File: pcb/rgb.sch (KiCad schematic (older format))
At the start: 14 parts, among them J1 Conn_02x08_Odd_Even, J2 Conn_01x06, J3 Conn_01x02, U1 ESP-WROOM-32, U2 LM317EMP, U3 RASPI_SD

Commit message: Minimum example to show 1 (sub)frame for debugging
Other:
- note added: "First prototype has B0 here"
- note added: "First prototype has D here"
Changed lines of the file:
@@
 	1    0    0    -1
 $EndComp
+Text Notes 7800 2600 0    60   ~ 0
+First prototype has D here
+Text Notes 6550 4200 3    60   ~ 0
+First prototype has B0 here
 $EndSCHEMATC

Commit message: SD card is online and integrated into webserver
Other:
- note added: "First prototype CS"
- note added: "REV1 CS"
- note added: "REV1 MISO"
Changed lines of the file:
@@
 U 1 1 5A206FDA
 P 5200 3200
-F 0 "R4" V 5100 3000 50  0000 C CNN
-F 1 "10k" V 5084 3200 50  0000 C CNN
+F 0 "R4" V 5300 3050 50  0000 C CNN
+F 1 "10k" V 5300 3250 50  0000 C CNN
 F 2 "Resistors_SMD:R_0805" V 5130 3200 50  0001 C CNN
 F 3 "" H 5200 3200 50  0001 C CNN
@@
 Text Notes 6550 4200 3    60   ~ 0
 First prototype has B0 here
+Text Notes 4550 3100 0    60   ~ 0
+First prototype CS
+Text Notes 5400 3700 0    60   ~ 0
+REV1 CS
+Text Notes 5300 3800 0    60   ~ 0
+REV1 MISO
 $EndSCHEMATC

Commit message: PCB REV1
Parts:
- removed J2: Conn_01x06, myStuff:myPogoPads, symbol rgb-rescue:Conn_01x06-RESCUE-rgb
- added C5: 1u, Capacitors_SMD:C_0805, symbol Device:C
- added J2: Conn_01x02, Pin_Headers:Pin_Header_Angled_1x02_Pitch2.54mm, symbol rgb-rescue:Conn_01x02-RESCUE-rgb
- added P1: TTL_232R_3V3, Pin_Headers:Pin_Header_Angled_1x06_Pitch2.54mm, symbol myStuff:TTL_232R_3V3
- added R6: 10k, Resistors_SMD:R_0805, symbol Device:R
- added U4, U5: TACTILE, myStuff:EVQQ2, symbol myStuff:TACTILE
- C4: renamed from C?; symbol device:C -> Device:C
- R2, R3: renamed from R?; footprint (none) -> Resistors_SMD:R_0805; symbol device:R -> Device:R
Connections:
- wire segments 91 -> 133
- no-connect marks 14 -> 13
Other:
- note added: "Flash"
- note added: "Photo\nresistor"
- note added: "Reset"
- note removed: "5 V"
- note removed: "First prototype CS"
- note removed: "First prototype has B0 here"
- note removed: "First prototype has D here"
- note removed: "GND"
- note removed: "REV1 CS"
- note removed: "REV1 MISO"
- note removed: "RXD"
- note removed: "Rst"
- note removed: "TXD"

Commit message: final pcb with second sd card slot and kicad 5
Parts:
- added U6: MicroSD_SPI_CD, newStuff:GCT-MEM2055-00-190-01-A, symbol microsd_spi_cd:MicroSD_SPI_CD
- C1, C2, C3: symbol rgb-rescue:C-RESCUE-rgb -> Device:C
- J1: symbol rgb-rescue:Conn_02x08_Odd_Even-RESCUE-rgb -> Connector_Generic:Conn_02x08_Odd_Even
- J2, J3: symbol rgb-rescue:Conn_01x02-RESCUE-rgb -> Connector_Generic:Conn_01x02
- R1, R4: symbol rgb-rescue:R-RESCUE-rgb -> Device:R
- U1: symbol rgb-rescue:ESP-WROOM-32-RESCUE-rgb -> myStuff:ESP-WROOM-32
- U2: symbol rgb-rescue:LM317EMP-RESCUE-rgb -> myStuff:LM317EMP
- U3: symbol rgb-rescue:RASPI_SD-RESCUE-rgb -> myStuff:RASPI_SD
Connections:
- wire segments 133 -> 139
- no-connect marks 13 -> 14
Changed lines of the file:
@@
 $EndDescr
 $Comp
-L rgb-rescue:+3V3-RESCUE-rgb #PWR01
+L power:+3.3V #PWR01
 U 1 1 5A1F09A4
 P 5400 2450
@@
 $EndComp
 $Comp
-L rgb-rescue:C-RESCUE-rgb C1
+L Device:C C1
 U 1 1 5A1F09A5
 P 5600 2500
@@
 $EndComp
 $Comp
-L rgb-rescue:GND-RESCUE-rgb #PWR02
+L power:GND #PWR02
 U 1 1 5A1F09A6
 P 5800 2500
@@
 $EndComp
 $Comp
-L rgb-rescue:GND-RESCUE-rgb #PWR03
+L power:GND #PWR03
 U 1 1 5A1F09A7
 P 7850 2450
@@
 $EndComp
 $Comp
-L rgb-rescue:ESP-WROOM-32-RESCUE-rgb U1
+L myStuff:ESP-WROOM-32 U1
 U 1 1 5A1F09A8
 P 6750 3150
@@
 $EndComp
 $Comp
-L rgb-rescue:R-RESCUE-rgb R1
+L Device:R R1
 U 1 1 5A1F09AB
 P 5200 2500
@@
 rstBtn
 $Comp
-L rgb-rescue:GND-RESCUE-rgb #PWR04
+L power:GND #PWR04
 U 1 1 5A1F09AC
 P 6400 4200
@@
 $EndComp
 $Comp
-L rgb-rescue:GND-RESCUE-rgb #PWR05
+L power:GND #PWR05
 U 1 1 5A1F09AD
 P 9400 3150
@@
 progFlag
 $Comp
-L rgb-rescue:LM317EMP-RESCUE-rgb U2
+L myStuff:LM317EMP U2
 U 1 1 5A1F2D82
 P 3100 6450
@@
 $EndComp
 $Comp
-L rgb-rescue:+3V3-RESCUE-rgb #PWR06
+L power:+3.3V #PWR06
 U 1 1 5A1F32B5
 P 4500 6350
@@
 $EndComp
 $Comp
-L rgb-rescue:GND-RESCUE-rgb #PWR07
+L power:GND #PWR07
 U 1 1 5A1F370A
 P 3950 7200
@@
 $EndComp
 $Comp
-L rgb-rescue:GND-RESCUE-rgb #PWR08
+L power:GND #PWR08
 U 1 1 5A1F3E37
 P 2550 7200
@@
 $EndComp
 $Comp
-L rgb-rescue:Conn_01x02-RESCUE-rgb J3
+L Connector_Generic:Conn_01x02 J3
 U 1 1 5A1F3E67
 P 1950 6750
@@
 $EndComp
 $Comp
-L rgb-rescue:GND-RESCUE-rgb #PWR09
+L power:GND #PWR09
 U 1 1 5A1F3FA2
 P 2200 7200
@@
 	2200 6400 2550 6400
 $Comp
-L rgb-rescue:C-RESCUE-rgb C3
+L Device:C C3
 U 1 1 5A1F4174
 P 2550 6850
@@
 5 V input
 $Comp
-L rgb-rescue:GND-RESCUE-rgb #PWR010
+L power:GND #PWR010
 U 1 1 5A1F44EA
 P 4500 7200
@@
 $EndComp
 $Comp
-L rgb-rescue:C-RESCUE-rgb C2
+L Device:C C2
 U 1 1 5A1F44F0
 P 4500 6800
@@
 	2200 6350 2200 6400
 $Comp
-L rgb-rescue:+5V-RESCUE-rgb #PWR011
+L power:+5V #PWR011
 U 1 1 5A1F57FC
 P 9400 3000
@@
 Connection ~ 2200 6400
 $Comp
-L rgb-rescue:Conn_02x08_Odd_Even-RESCUE-rgb J1
+L Connector_Generic:Conn_02x08_Odd_Even J1
 U 1 1 5A1F6343
 P 2050 2600
@@
 Connection ~ 2200 7100
 $Comp
-L rgb-rescue:RASPI_SD-RESCUE-rgb U3
+L myStuff:RASPI_SD U3
 U 1 1 5A2024AA
 P 2850 5350
@@
 SD_CLK
 $Comp
-L rgb-rescue:R-RESCUE-rgb R4
+L Device:R R4
 U 1 1 5A206FDA
 P 5200 3200
@@
 $EndComp
 $Comp
-L rgb-rescue:+3V3-RESCUE-rgb #PWR019
+L power:+3.3V #PWR019
 U 1 1 5A207217
 P 5000 3200
@@
 	9350 3800 9350 3700
 $Comp
-L rgb-rescue:GND-RESCUE-rgb #PWR024
+L power:GND #PWR024
 U 1 1 5A942877
 P 9850 3750
@@
 	9350 2050 9400 2050
 $Comp
-L rgb-rescue:GND-RESCUE-rgb #PWR023
+L power:GND #PWR023
 U 1 1 5A95FB89
 P 9850 2100
@@
 $EndComp
 $Comp
-L rgb-rescue:+3V3-RESCUE-rgb #PWR020
+L power:+3.3V #PWR020
 U 1 1 5A9EBD96
 P 4100 2400
@@
 	2200 6400 2200 6750
 $Comp
-L rgb-rescue:Conn_01x02-RESCUE-rgb J2
+L Connector_Generic:Conn_01x02 J2
 U 1 1 5AA1C52F
 P 3900 2550
@@
 Text Notes 3950 2450 2    60   ~ 0
 Photo\nresistor
+$Comp
+L microsd_spi_cd:MicroSD_SPI_CD U6
+U 1 1 5ABB763C
+P 4350 4250
+F 0 "U6" H 4073 4303 60  0000 R CNN
+F 1 "MicroSD_SPI_CD" H 4073 4197 60  0000 R CNN
+F 2 "newStuff:GCT-MEM2055-00-190-01-A" H 4073 4144 60  0001 R CNN
+F 3 "" H 4200 4250 60  0000 C CNN
+	1    4350 4250
+	-1   0    0    -1
+$EndComp
+Wire Wire Line
+	3550 4450 4000 4450
+Text Label 3550 4450 0    60   ~ 0
+SD_MISO
+Wire Wire Line
+	3550 3950 4000 3950
+Text Label 3600 3950 0    60   ~ 0
+SD_CS
+Wire Wire Line
+	3550 4050 4000 4050
+Text Label 3600 4050 0    60   ~ 0
+SD_MOSI
+Wire Wire Line
+	3550 4250 4000 4250
+Text Label 3600 4250 0    60   ~ 0
+SD_CLK
+$Comp
+L power:GND #PWR026
+U 1 1 5ABEF3D1
+P 3950 4350
+F 0 "#PWR026" H 3950 4100 50  0001 C CNN
+F 1 "GND" V 3950 4150 50  0000 C CNN
+F 2 "" H 3950 4350 50  0001 C CNN
+F 3 "" H 3950 4350 50  0001 C CNN
+	1    3950 4350
+	0    1    1    0
+$EndComp
+$Comp
+L power:+3V3 #PWR025
+U 1 1 5ABEF562
+P 3950 4150
+F 0 "#PWR025" H 3950 4000 50  0001 C CNN
+F 1 "+3V3" V 3950 4400 50  0000 C CNN
+F 2 "" H 3950 4150 50  0001 C CNN
+F 3 "" H 3950 4150 50  0001 C CNN
+	1    3950 4150
+	0    -1   -1   0
+$EndComp
+Wire Wire Line
+	3950 4150 4000 4150
+Wire Wire Line
+	3950 4350 4000 4350
+NoConn ~ 4000 4550
 $EndSCHEMATC

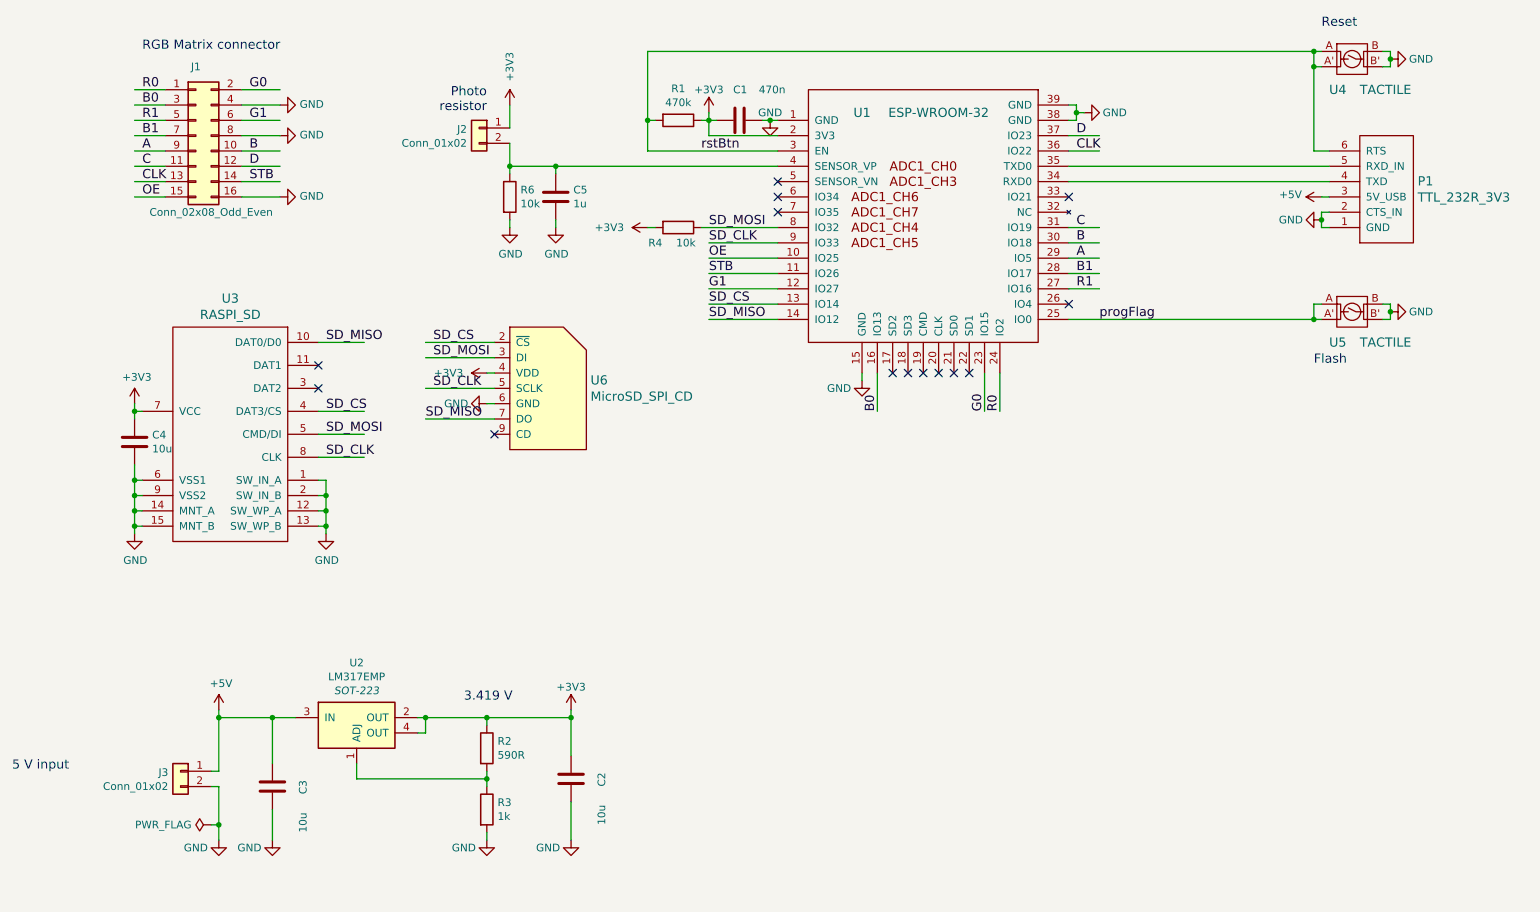
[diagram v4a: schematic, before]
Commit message: pcb: fix value of V-REG, Add info about SD card sockets
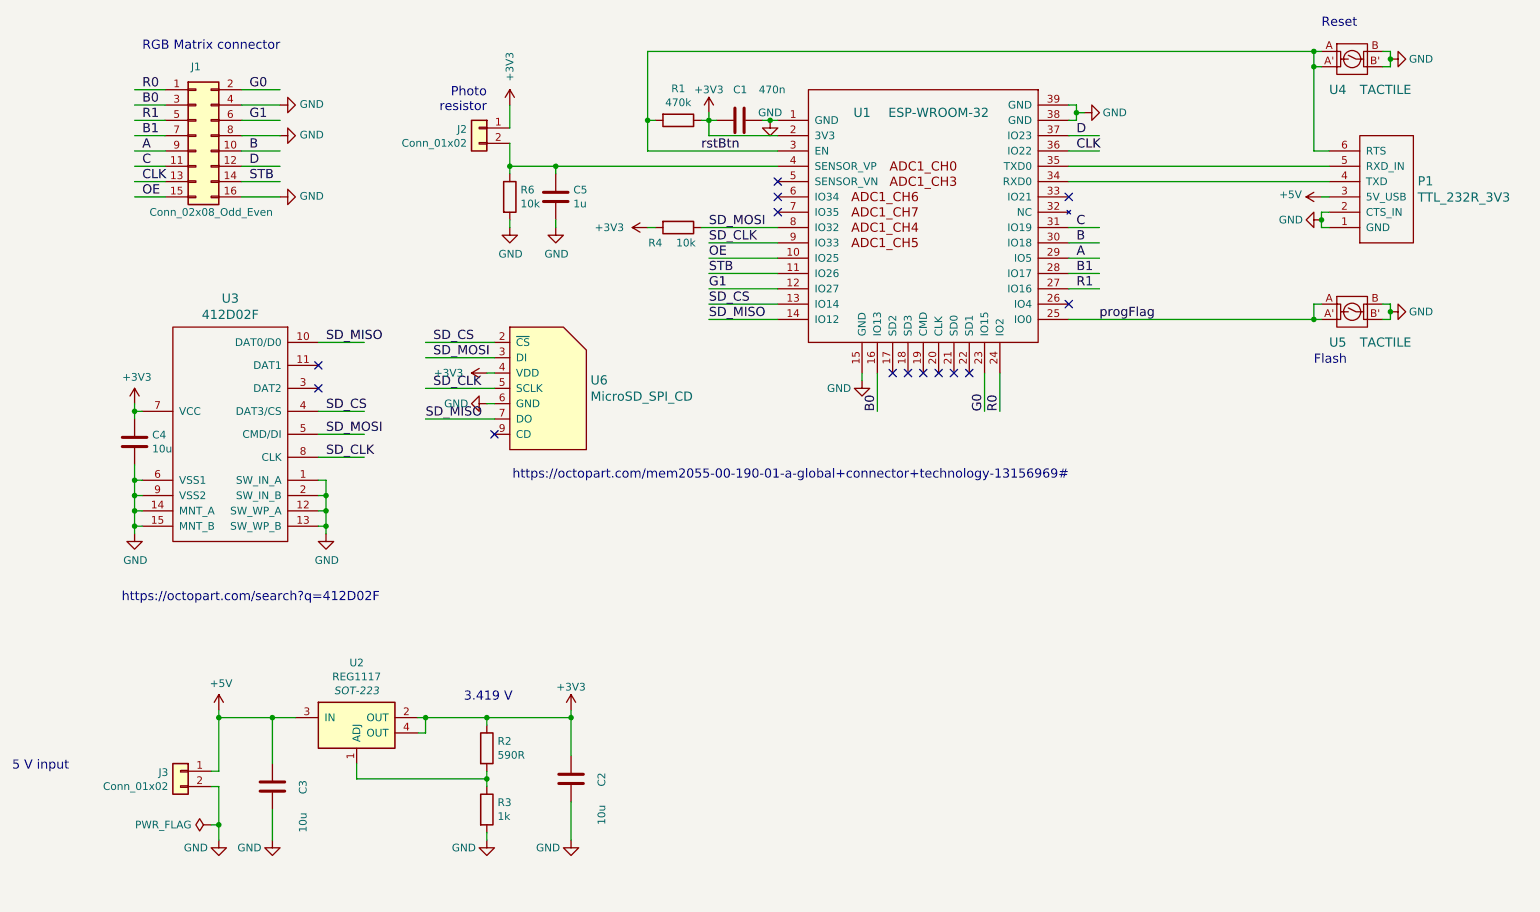
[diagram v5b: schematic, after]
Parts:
- U2: value LM317EMP -> REG1117
- U3: value RASPI_SD -> 412D02F
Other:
- note added: "https://octopart.com/mem2055-00-190-01-a-global+connector+technology-13156969#"
- note added: "https://octopart.com/search?q=412D02F"

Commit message: pcb: clean up project. Make kicad 5.1.x compatible
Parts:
- P1: symbol myStuff:TTL_232R_3V3 -> rgb-rescue:TTL_232R_3V3-myStuff
- U1: symbol myStuff:ESP-WROOM-32 -> rgb-rescue:ESP-WROOM-32-myStuff
- U2: symbol myStuff:LM317EMP -> rgb-rescue:LM317EMP-myStuff
- U3: symbol myStuff:RASPI_SD -> rgb-rescue:RASPI_SD-myStuff
- U4, U5: symbol myStuff:TACTILE -> rgb-rescue:TACTILE-myStuff
- U6: symbol microsd_spi_cd:MicroSD_SPI_CD -> rgb-rescue:MicroSD_SPI_CD-microsd_spi_cd
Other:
- note added: "TODO for REV 2:\n* optional 5v level translation\n* corrected pinout for the IDC connector\n* enough room for the shroud of the IDC connector\n* move SD MISO pin to GPIO 35 (boot issue)\n* use a more common v-reg / SD card socket"
